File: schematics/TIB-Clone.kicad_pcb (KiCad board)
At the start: 2 copper layers, 91.4 x 58.4 mm, 28 parts, among them CN1 FLOPPY CONNECTOR, J1 MO1, J2 MO2, J3 DS1, J4 DS2, Q1 16.000, U1 2764, U2 74LS00, U3 74LS00, U4 WD37C65

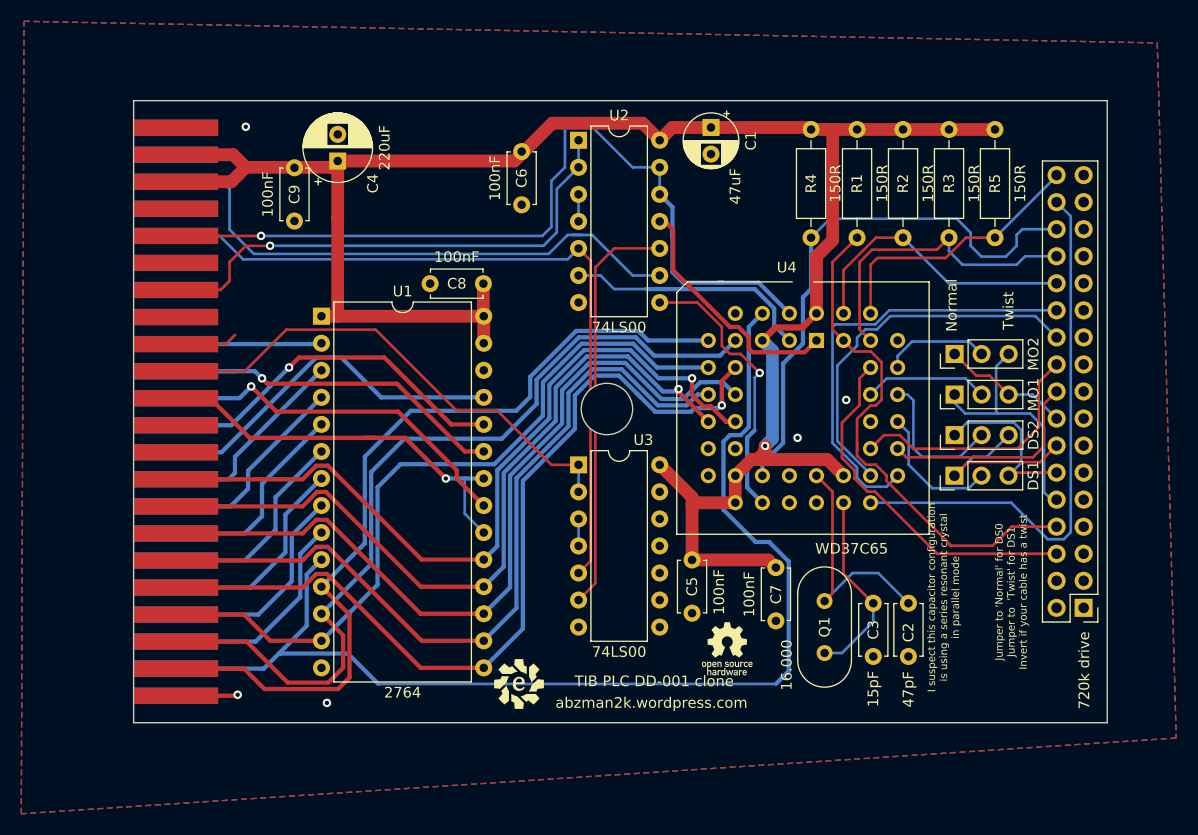
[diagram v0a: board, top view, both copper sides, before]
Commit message: fixed traces, DRC, gerbers
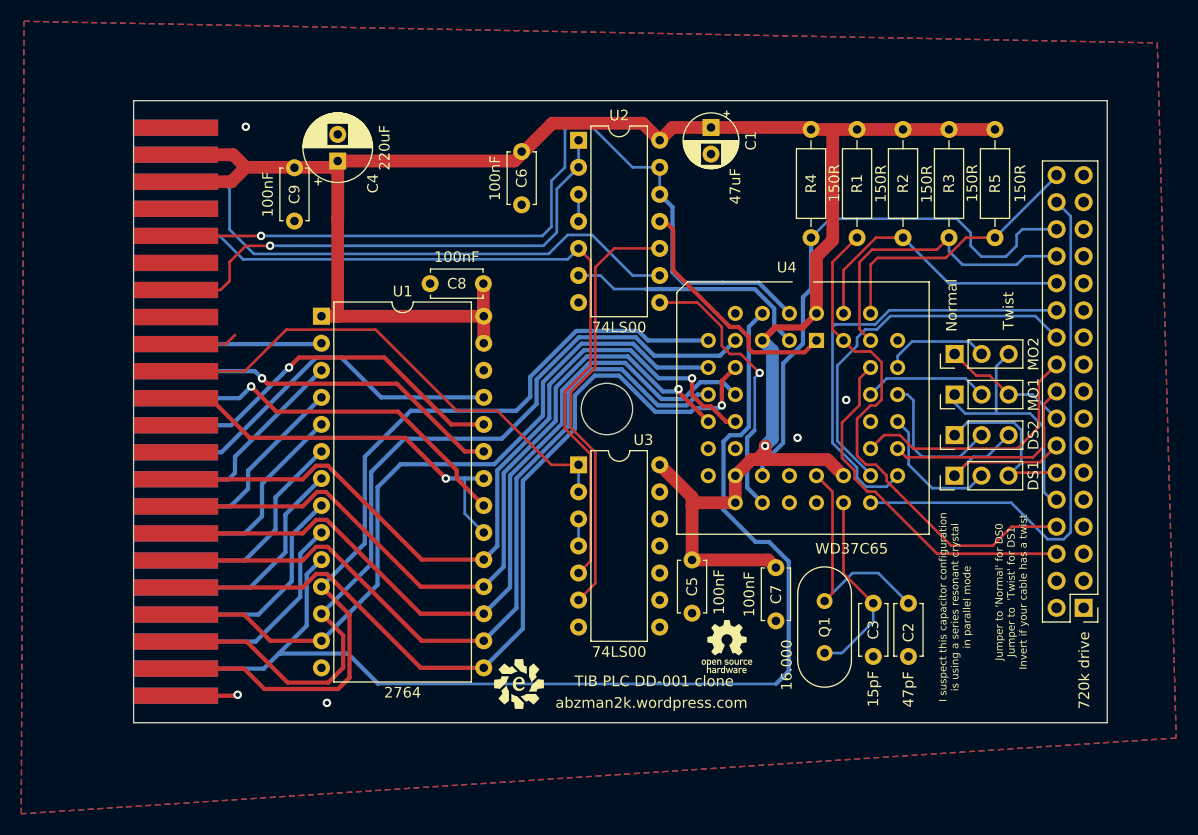
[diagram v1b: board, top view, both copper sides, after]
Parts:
- moved G*** 0.20 mm to (185.4, 98.3)
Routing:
- net A11: track 37.8 -> 32.1 mm
- net *FCS: track 28.8 -> 23.2 mm
- net *RDD: track 54.4 -> 51.9 mm
- net PHI2: track 70.6 -> 72.6 mm
- net Net-(U3-Pad6): track 38.7 -> 40.6 mm
- net *FWR: track 80.1 -> 78.8 mm
- net ROML: track 38.9 -> 37.9 mm
- net *IDX: track 49.6 -> 48.8 mm
- net ~{RESET}: track 53.7 -> 52.8 mm
- net D3: track 83.1 -> 82.6 mm
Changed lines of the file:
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@@
       (layerselection 0x00010fc_ffffffff)
       (disableapertmacros false)
-      (usegerberextensions false)
+      (usegerberextensions true)
       (usegerberattributes true)
       (usegerberadvancedattributes true)
@@
       (plotinvisibletext false)
       (sketchpadsonfab false)
-      (subtractmaskfromsilk false)
+      (subtractmaskfromsilk true)
       (outputformat 1)
       (mirror false)
-      (drillshape 1)
+      (drillshape 0)
       (scaleselection 1)
-      (outputdirectory "")
+      (outputdirectory "TIB-Clone-gerbers")
     )
   )
@@
       (effects (font (size 1 1) (thickness 0.15)))
     )
-    (fp_text value "150R" (at 5.08 2.37 90) (layer "F.SilkS")
+    (fp_text value "150R" (at 5.0292 2.2352 90) (layer "F.SilkS")
       (effects (font (size 1 1) (thickness 0.15)))
     )
@@
       (effects (font (size 1 1) (thickness 0.15)))
     )
-    (fp_text value "150R" (at 5.08 2.37 90) (layer "F.SilkS")
+    (fp_text value "150R" (at 5.1054 2.1844 90) (layer "F.SilkS")
       (effects (font (size 1 1) (thickness 0.15)))
     )
@@
   )
   (footprint "Evan's misc parts:OSHW gear" (layer "F.Cu")
-    (at 185.42 98.552)
+    (at 185.3946 98.3488)
     (attr board_only exclude_from_pos_files exclude_from_bom)
     (fp_text reference "G***" (at 0 5.08) (layer "F.Fab") hide
@@
       (effects (font (size 1 1) (thickness 0.15)))
     )
-    (fp_text value "150R" (at 5.08 -2.286 90) (layer "F.SilkS")
+    (fp_text value "150R" (at 5.0546 -2.1844 90) (layer "F.SilkS")
       (effects (font (size 1 1) (thickness 0.15)))
     )
@@
       (effects (font (size 1 1) (thickness 0.15)))
     )
-    (fp_text value "150R" (at 5.08 2.37 90) (layer "F.SilkS")
+    (fp_text value "150R" (at 5.0546 2.2352 90) (layer "F.SilkS")
       (effects (font (size 1 1) (thickness 0.15)))
     )
@@
     (effects (font (size 1 1) (thickness 0.15)))
   )
-  (gr_text "I suspect this capacitor configuration\nis using a series resonant crystal\nin parallel mode" (at 205.74 93.726 90) (layer "F.SilkS")
+  (gr_text "I suspect this capacitor configuration\nis using a series resonant crystal\nin parallel mode" (at 206.8068 94.6404 90) (layer "F.SilkS")
     (effects (font (size 0.7 0.7) (thickness 0.1)))
   )
@@
   (segment (start 196.196266 80.626266) (end 196.196266 77.322312) (width 0.25) (layer "F.Cu") (net 7))
   (segment (start 197.377711 81.807711) (end 196.196266 80.626266) (width 0.25) (layer "F.Cu") (net 7))
-  (segment (start 197.612 79.950718) (end 197.612 79.248) (width 0.25) (layer "F.Cu") (net 8))
   (segment (start 197.612 79.248) (end 197.612 80.419296) (width 0.25) (layer "F.Cu") (net 8))
   (segment (start 197.377711 70.631711) (end 196.342 69.596) (width 0.25) (layer "F.Cu") (net 8))
@@
   (segment (start 200.386289 82.784289) (end 201.295 83.693) (width 0.25) (layer "F.Cu") (net 8))
   (segment (start 206.464511 88.862511) (end 210.349489 88.862511) (width 0.25) (layer "F.Cu") (net 8))
-  (segment (start 206.285489 88.862511) (end 206.464511 88.862511) (width 0.25) (layer "F.Cu") (net 8))
   (segment (start 199.917711 71.647711) (end 198.901711 70.631711) (width 0.25) (layer "F.Cu") (net 8))
   (segment (start 200.386289 82.276289) (end 200.386289 82.784289) (width 0.25) (layer "F.Cu") (net 8))
@@
   (segment (start 215.0005 75.5755) (end 214.101 74.676) (width 0.25) (layer "B.Cu") (net 12))
   (segment (start 214.101 74.676) (end 211.851 74.676) (width 0.25) (layer "B.Cu") (net 12))
-  (segment (start 215.0005 75.5755) (end 214.884 75.459) (width 0.25) (layer "B.Cu") (net 12))
   (segment (start 215.138 79.56048) (end 215.138 75.602) (width 0.25) (layer "F.Cu") (net 13))
   (segment (start 214.122 80.57648) (end 215.138 79.56048) (width 0.25) (layer "F.Cu") (net 13))
@@
   (segment (start 206.248 61.214) (end 207.518 62.484) (width 0.25) (layer "B.Cu") (net 18))
   (segment (start 207.518 62.484) (end 212.598 62.484) (width 0.25) (layer "B.Cu") (net 18))
-  (segment (start 193.294 62.484) (end 193.294 59.944) (width 0.25) (layer "B.Cu") (net 19))
   (segment (start 206.973022 58.166) (end 208.28 59.472978) (width 0.25) (layer "B.Cu") (net 19))
   (segment (start 212.598 60.706) (end 212.598 59.69) (width 0.25) (layer "B.Cu") (net 19))
@@
   (via (at 141.6445 59.7775) (size 0.8) (drill 0.4) (layers "F.Cu" "B.Cu") (net 23))
   (segment (start 170.475978 49.53) (end 172.72 49.53) (width 0.25) (layer "B.Cu") (net 23))
-  (segment (start 180.279511 59.883511) (end 180.279511 58.988489) (width 0.4) (layer "B.Cu") (net 23))
   (segment (start 188.37648 64.17048) (end 191.262 67.056) (width 0.4) (layer "B.Cu") (net 23))
   (segment (start 180.279511 63.185511) (end 180.279511 58.988489) (width 0.4) (layer "B.Cu") (net 23))
@@
   (segment (start 168.91 54.61) (end 170.18 53.34) (width 0.25) (layer "B.Cu") (net 23))
   (segment (start 170.18 53.34) (end 170.18 49.825978) (width 0.25) (layer "B.Cu") (net 23))
-  (segment (start 184.56648 64.17048) (end 185.00352 64.17048) (width 0.4) (layer "B.Cu") (net 23))
   (segment (start 179.08 55.875) (end 179.08 53.335) (width 0.25) (layer "B.Cu") (net 23))
   (segment (start 168.0605 59.7775) (end 141.6445 59.7775) (width 0.25) (layer "B.Cu") (net 23))
@@
   (segment (start 140.571274 78.74) (end 151.384 78.74) (width 0.4) (layer "F.Cu") (net 28))
   (segment (start 155.174 78.74) (end 151.384 78.74) (width 0.4) (layer "F.Cu") (net 28))
-  (segment (start 151.384 78.74) (end 152.4 78.74) (width 0.4) (layer "F.Cu") (net 28))
   (segment (start 133.610774 75.0175) (end 136.848774 75.0175) (width 0.4) (layer "F.Cu") (net 28))
   (segment (start 136.848774 75.0175) (end 140.571274 78.74) (width 0.4) (layer "F.Cu") (net 28))
@@
   (segment (start 184.912 75.692) (end 184.658 75.946) (width 0.4) (layer "B.Cu") (net 35))
   (segment (start 176.911 74.549) (end 178.653521 76.29152) (width 0.4) (layer "B.Cu") (net 35))
-  (segment (start 177.292 74.93) (end 176.911 74.549) (width 0.4) (layer "B.Cu") (net 35))
   (segment (start 184.658 75.946) (end 182.372 75.946) (width 0.4) (layer "B.Cu") (net 35))
   (segment (start 166.22808 82.78132) (end 166.22808 96.66692) (width 0.4) (layer "B.Cu") (net 35))
@@
   (segment (start 140.97 61.468) (end 138.684 59.182) (width 0.25) (layer "B.Cu") (net 40))
   (segment (start 172.73 59.69) (end 176.535 63.495) (width 0.25) (layer "B.Cu") (net 40))
-  (segment (start 171.7853 59.69) (end 170.942 59.69) (width 0.25) (layer "B.Cu") (net 40))
   (segment (start 172.584511 90.310489) (end 171.46 91.435) (width 0.25) (layer "F.Cu") (net 42))
-  (segment (start 172.584511 62.079511) (end 172.584511 90.310489) (width 0.25) (layer "F.Cu") (net 42))
+  (segment (start 172.584511 80.280911) (end 172.584511 90.310489) (width 0.25) (layer "F.Cu") (net 42))
+  (segment (start 172.584511 71.975111) (end 170.1673 74.392322) (width 0.25) (layer "F.Cu") (net 42))
+  (segment (start 172.584511 62.079511) (end 172.584511 71.975111) (width 0.25) (layer "F.Cu") (net 42))
+  (segment (start 170.1673 74.392322) (end 170.1673 77.8637) (width 0.25) (layer "F.Cu") (net 42))
+  (segment (start 170.1673 77.8637) (end 172.584511 80.280911) (width 0.25) (layer "F.Cu") (net 42))
   (segment (start 171.46 60.955) (end 172.584511 62.079511) (width 0.25) (layer "F.Cu") (net 42))
   (segment (start 133.610774 59.7775) (end 137.7555 59.7775) (width 0.25) (layer "B.Cu") (net 42))
@@
   (segment (start 160.772 80.02) (end 162.555 80.02) (width 0.4) (layer "F.Cu") (net 47))
   (via (at 141.732 73.152) (size 0.8) (drill 0.4) (layers "F.Cu" "B.Cu") (net 47))
-  (segment (start 133.610774 72.4775) (end 139.3585 72.4775) (width 0.4) (layer "B.Cu") (net 47))
   (segment (start 141.732 73.152) (end 141.0575 72.4775) (width 0.4) (layer "B.Cu") (net 47))
   (segment (start 141.0575 72.4775) (end 133.610774 72.4775) (width 0.4) (layer "B.Cu") (net 47))
@@
   (segment (start 187.292711 78.731139) (end 188.002925 78.020925) (width 0.4) (layer "B.Cu") (net 64))
   (segment (start 171.46 55.875) (end 171.46 58.415) (width 0.25) (layer "B.Cu") (net 65))
-  (segment (start 174.817031 60.955) (end 179.08 60.955) (width 0.25) (layer "F.Cu") (net 66))
-  (segment (start 173.034031 92.400969) (end 173.034031 62.738) (width 0.25) (layer "F.Cu") (net 66))
-  (segment (start 173.034031 62.738) (end 174.817031 60.955) (width 0.25) (layer "F.Cu") (net 66))
-  (segment (start 171.46 93.975) (end 173.034031 92.400969) (width 0.25) (layer "F.Cu") (net 66))
+  (segment (start 174.817031 60.955) (end 173.034031 62.738) (width 0.25) (layer "F.Cu") (net 66))
+  (segment (start 173.034031 72.161309) (end 170.739159 74.456181) (width 0.25) (layer "F.Cu") (net 66))
+  (segment (start 173.034031 92.400969) (end 171.46 93.975) (width 0.25) (layer "F.Cu") (net 66))
+  (segment (start 170.739159 74.456181) (end 170.739159 77.799841) (width 0.25) (layer "F.Cu") (net 66))
+  (segment (start 170.739159 77.799841) (end 173.034031 80.094713) (width 0.25) (layer "F.Cu") (net 66))
+  (segment (start 173.034031 80.094713) (end 173.034031 92.400969) (width 0.25) (layer "F.Cu") (net 66))
+  (segment (start 179.08 60.955) (end 174.817031 60.955) (width 0.25) (layer "F.Cu") (net 66))
+  (segment (start 173.034031 62.738) (end 173.034031 72.161309) (width 0.25) (layer "F.Cu") (net 66))
   (segment (start 185.674 68.326) (end 180.34 62.992) (width 0.4) (layer "F.Cu") (net 67))
   (segment (start 187.800711 70.706711) (end 187.452 70.358) (width 0.4) (layer "F.Cu") (net 67))
@@
   (segment (start 173.523978 63.495) (end 171.46 63.495) (width 0.25) (layer "B.Cu") (net 68))
   (segment (start 189.832711 68.166711) (end 189.832711 66.595927) (width 0.4) (layer "B.Cu") (net 68))
-  (segment (start 183.388 64.77) (end 177.8 64.77) (width 0.25) (layer "B.Cu") (net 68))
   (segment (start 174.798978 64.77) (end 173.523978 63.495) (width 0.25) (layer "B.Cu") (net 68))
   (segment (start 171.46 86.355) (end 171.46 88.895) (width 0.25) (layer "B.Cu") (net 70))
